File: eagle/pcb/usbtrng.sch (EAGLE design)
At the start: 37 parts, among them IC1 FT232RL, IC2 ATMEGA88, IC3 XC9572XL VQ44, IC4 LT1763CS8-3.3, J1 CON_HEADER_2X03-PTH, J2 CON_HEADER_1X06-PTH, J3 CON_HEADER_1X05-PTH, J5 CON_HEADER_1X01-PTH, J7 CON_HEADER_1X01-PTH, J8 CON_HEADER_1X01-PTH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

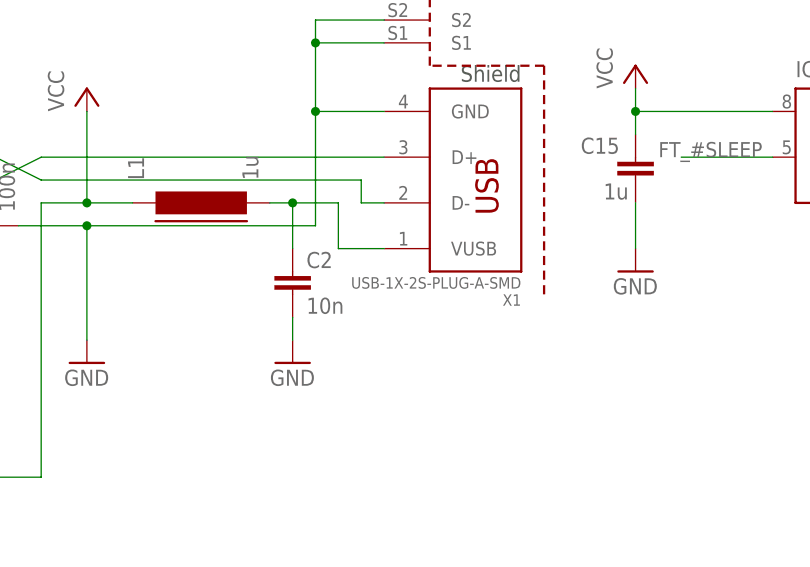
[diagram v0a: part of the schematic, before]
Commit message: major revision of board layout
* better signal routing around ft232rl
* better placement of blockng capacitors
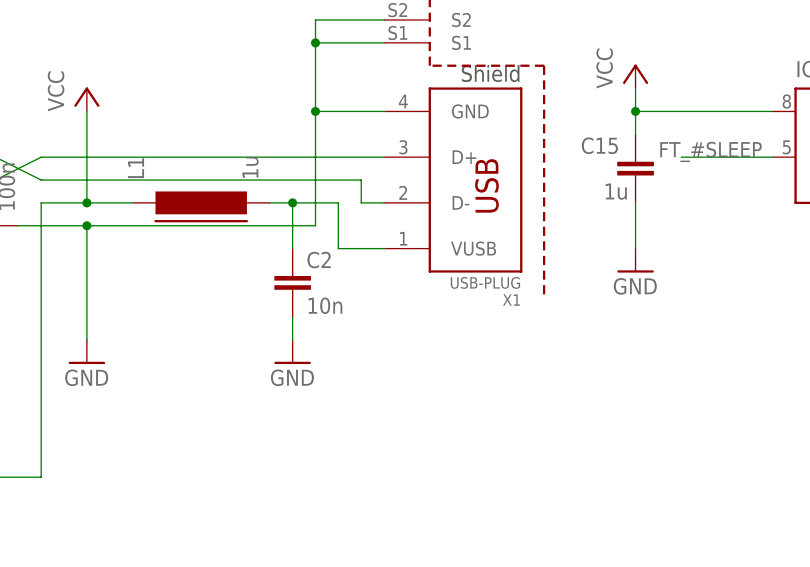
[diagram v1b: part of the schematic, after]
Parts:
- X1: value USB-1X-2S-PLUG-A-SMD -> USB-PLUG
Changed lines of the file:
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@@
 <part name="+3V12" library="supply1" deviceset="+3V3" device=""/>
 <part name="P+1" library="supply1" deviceset="VCC" device=""/>
-<part name="X1" library="_con-usb_1" deviceset="USB-1X-2S" device="-PLUG-A-SMD"/>
+<part name="X1" library="_con-usb_1" deviceset="USB-1X-2S" device="-PLUG-A-SMD" value="USB-PLUG"/>
 </parts>
 <sheets>

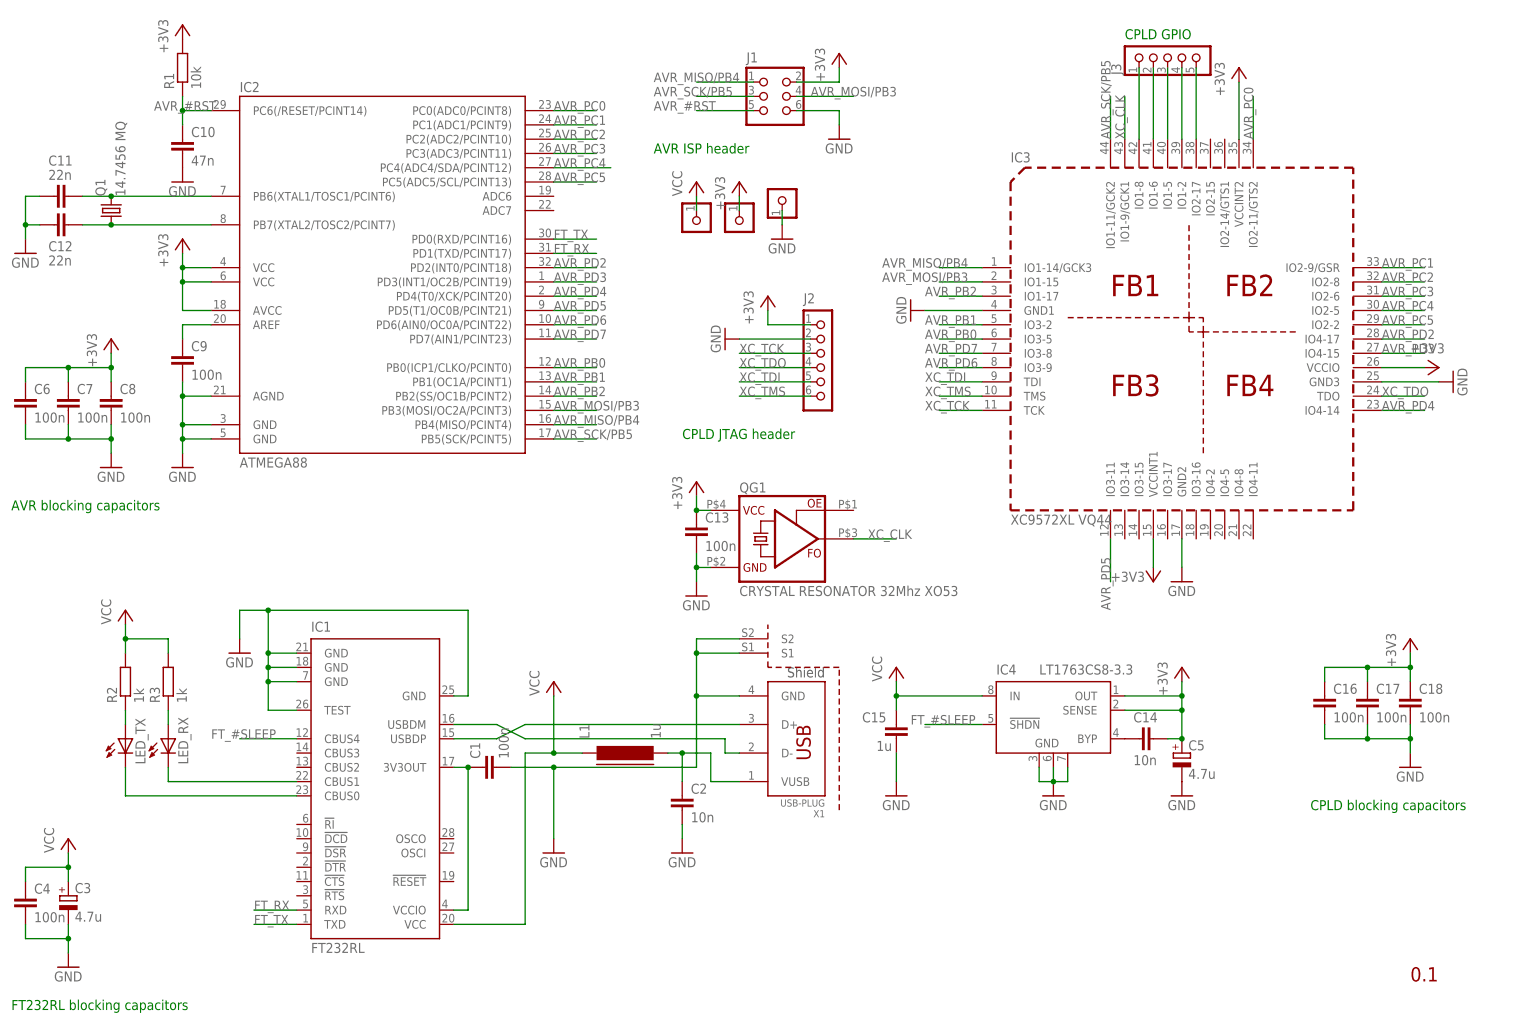
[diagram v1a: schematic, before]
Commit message: This is the revision, that is manufactured at q-print, v.0.1
* integrated 32 Mbit SPI-Flash, connected to the CPLD
* The rx/tx leds are now powerd by VCCIO
* further layout optimisations
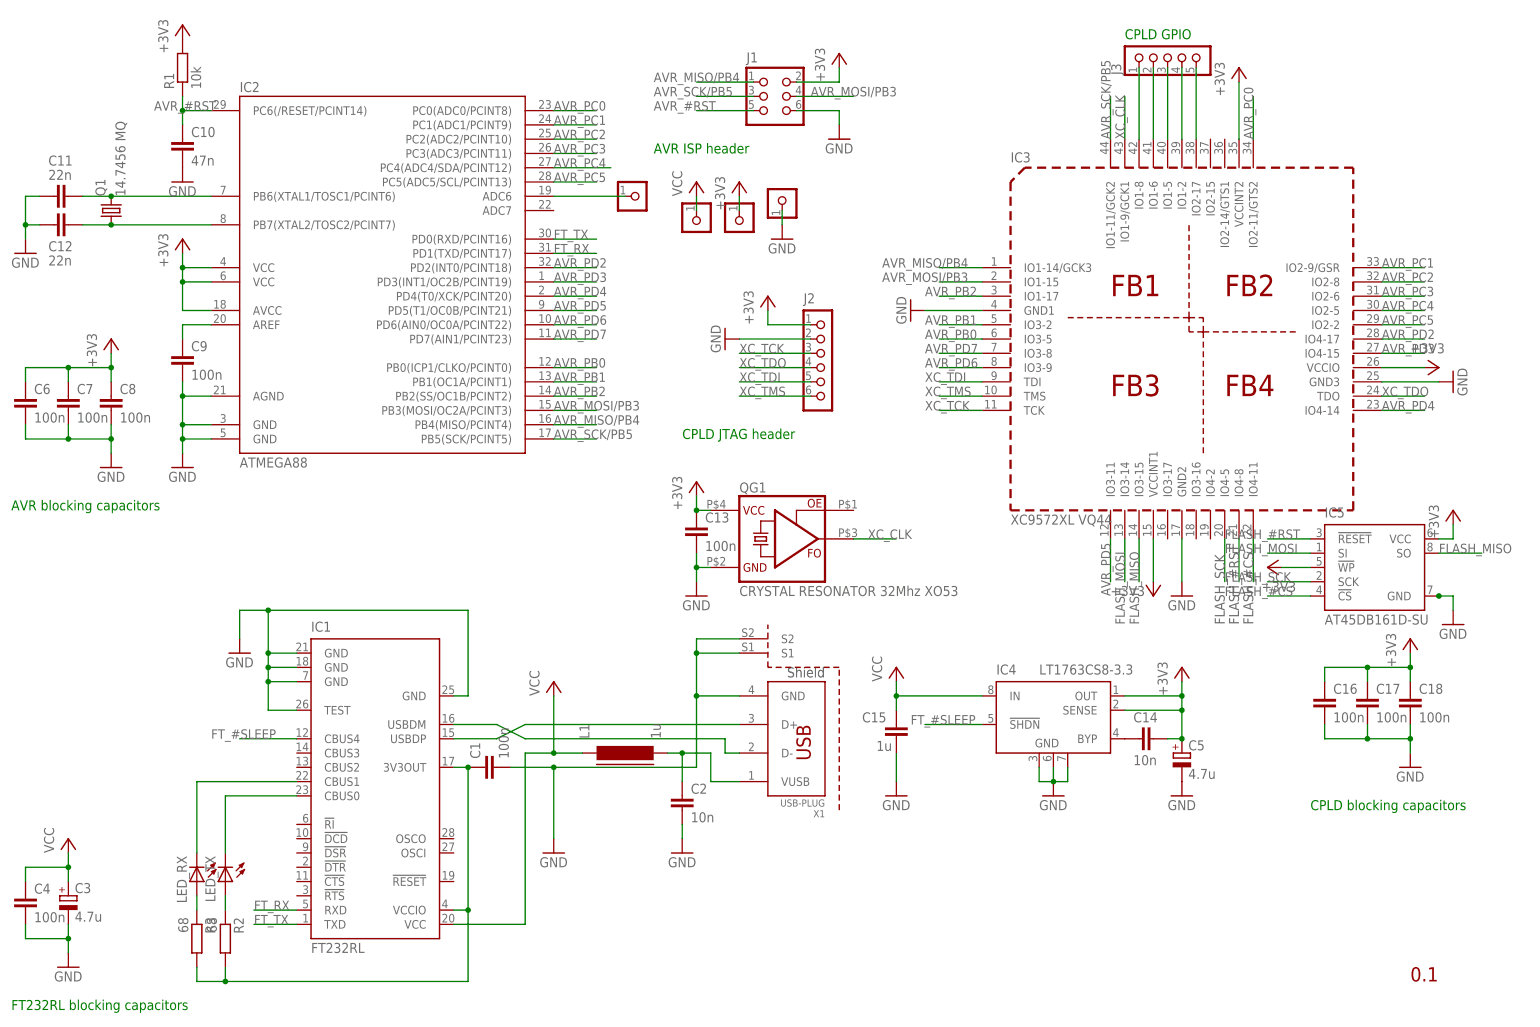
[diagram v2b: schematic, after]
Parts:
- added IC5: AT45DB161D-SU, atmel:AT45DB161D-SU
- added J4: CON_HEADER_1X01-PTH, dp_devices:CON_HEADER_1X01-PTH
- R2, R3: value 1k -> 68
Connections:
- new net FLASH_#CS: IC3.IO4-11, IC5.!CS
- new net FLASH_#RST: IC3.IO4-8, IC5.!RESET
- new net FLASH_MISO: IC3.IO3-15, IC5.SO
- new net FLASH_MOSI: IC3.IO3-14, IC5.SI
- new net FLASH_SCK: IC3.IO4-5, IC5.SCK
- new net N$18: IC2.ADC6, J4.1
- net +3V3: now also IC5.!WP, IC5.VCC
- net GND: now also IC5.GND
- net N$6: now also R2.2, R3.2
- net VCC: no longer R2.2, R3.2
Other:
- moved on the sheet: LED_RX, LED_TX, R2, R3
